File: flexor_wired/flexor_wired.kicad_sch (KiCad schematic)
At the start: 0 parts

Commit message: feat: add project metadata to KiCad files
- Add comments, revision, title and issue date to schematic and PCB
- Update project information for flexor_wired variant
- Update project information for flexor_wireless variant
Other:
- title: (none) -> Flexor Keyboard - Wired
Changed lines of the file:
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@@
 	(generator_version "9.0")
 	(paper "A4")
+	(title_block
+		(title "Flexor Keyboard - Wired")
+		(date "2025-08-14")
+		(rev "A")
+		(comment 1 "Wired Version")
+		(comment 2 "34-Key Split Ergonomic Keyboard")
+		(comment 4 "F L E X O R")
+	)
 	(sheet_instances
 		(path "/"

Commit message: feat: update PCB design and project configuration
- Update flexor_wired PCB layout and schematic
- Update project configuration and preferences
- Update footprint info cache
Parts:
- added D1, D10, D11, D12, D13, D14, D15, D16, D17, D18, D19, D2, D20, D21, D22, D23, D24, D25, D26, D27, D28, D29, D3, D30, D31, D32, D33, D34, D4, D5, D6, D7, D8, D9: 1N4148W, Diode:1N4148W_SOD-123_SMD, symbol Device:D_Small
- added H1, H2, H3, H4, H5, H6, H7, H8: MountingHole, Mounting_Hole:3.2mm_M3_DIN965_Pad, symbol Mechanical:MountingHole
- added SW1, SW10, SW11, SW12, SW13, SW14, SW15, SW16, SW17, SW18, SW19, SW2, SW20, SW21, SW22, SW23, SW24, SW25, SW26, SW27, SW28, SW29, SW3, SW30, SW31, SW32, SW33, SW34, SW4, SW5, SW6, SW7, SW8, SW9: PG1350, Kailh:PG1350_Choc_V1, symbol Switch:SW_Push
- added U1, U2: RP2040, Seed Studio:XIAO_RP2040_SMD, symbol Seed Studio:XIAO-RP2040-SMD
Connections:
- new net: D8.2 (A), SW8.2
- new net: D25.2 (A), SW25.2
- new net: D22.2 (A), SW22.2
- new net: D3.2 (A), SW3.2
- new net: D9.2 (A), SW9.2
- new net: D10.2 (A), SW10.2
- new net: D29.2 (A), SW29.2
- new net: D28.2 (A), SW28.2
- new net: D5.2 (A), SW5.2
- new net: D30.2 (A), SW30.2
- new net: D31.2 (A), SW31.2
- new net: D32.2 (A), SW32.2
- new net: D13.2 (A), SW13.2
- new net: D15.2 (A), SW15.2
- new net: D24.2 (A), SW24.2
- new net: D1.2 (A), SW1.2
- new net: D21.2 (A), SW21.2
- new net: D34.2 (A), SW34.2
- new net: D33.2 (A), SW33.2
- new net: D27.2 (A), SW27.2
- new net: D4.2 (A), SW4.2
- new net: D20.2 (A), SW20.2
- new net: D23.2 (A), SW23.2
- new net: D19.2 (A), SW19.2
- new net: D16.2 (A), SW16.2
- new net: D7.2 (A), SW7.2
- new net: D12.2 (A), SW12.2
- new net: D2.2 (A), SW2.2
- new net: D14.2 (A), SW14.2
- new net: D18.2 (A), SW18.2
- new net: D11.2 (A), SW11.2
- new net: D6.2 (A), SW6.2
- new net: D17.2 (A), SW17.2
- new net: D26.2 (A), SW26.2
- new net COL0_L: SW1.1, SW11.1, SW6.1, U1.5 (D4_SDA)
- new net COL0_R: SW22.1, SW27.1, SW32.1, U2.5 (D4_SDA)
- new net COL1_L: SW12.1, SW2.1, SW7.1, U1.6 (D5_SCL)
- new net COL1_R: SW21.1, SW26.1, SW31.1, U2.6 (D5_SCL)
- new net COL2_L: SW13.1, SW3.1, SW8.1, U1.11 (D10_MOSI)
- new net COL2_R: SW20.1, SW25.1, SW30.1, U2.11 (D10_MOSI)
- new net COL3_L: SW14.1, SW16.1, SW4.1, SW9.1, U1.10 (D9_MISO)
- new net COL3_R: SW19.1, SW24.1, SW29.1, SW34.1, U2.10 (D9_MISO)
- new net COL4_L: SW10.1, SW15.1, SW17.1, SW5.1, U1.9 (D8_SCK)
- new net COL4_R: SW18.1, SW23.1, SW28.1, SW33.1, U2.9 (D8_SCK)
- new net GND_L: U1.13 (GND)
- new net ROW0_L: D1.1 (K), D2.1 (K), D3.1 (K), D4.1 (K), D5.1 (K), U1.1 (D0)
- new net ROW0_R: D18.1 (K), D19.1 (K), D20.1 (K), D21.1 (K), D22.1 (K), U2.1 (D0)
- new net ROW1_L: D10.1 (K), D6.1 (K), D7.1 (K), D8.1 (K), D9.1 (K), U1.2 (D1)
- new net ROW1_R: D23.1 (K), D24.1 (K), D25.1 (K), D26.1 (K), D27.1 (K), U2.2 (D1)
- new net ROW2_L: D11.1 (K), D12.1 (K), D13.1 (K), D14.1 (K), D15.1 (K), U1.3 (D2)
- new net ROW2_R: D28.1 (K), D29.1 (K), D30.1 (K), D31.1 (K), D32.1 (K), U2.3 (D2)
- new net ROW3_L: D16.1 (K), D17.1 (K), U1.4 (D3)
- new net ROW3_R: D33.1 (K), D34.1 (K), U2.4 (D3)

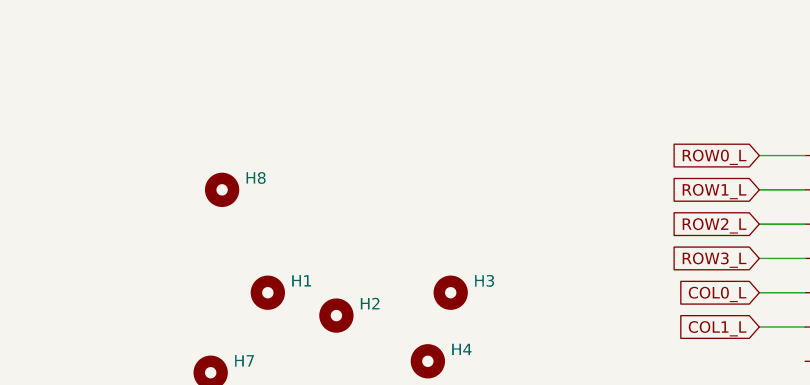
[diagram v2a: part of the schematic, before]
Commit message: feat(schematic): update schematic to support new keycap layout
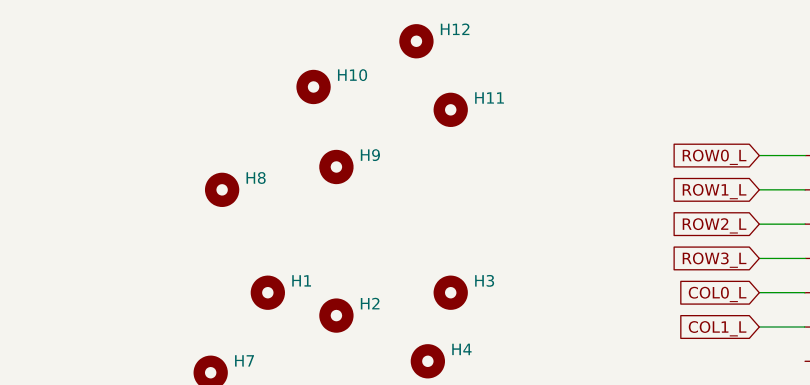
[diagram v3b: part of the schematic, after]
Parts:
- added H10, H11, H12, H9: MountingHole, Mounting_Hole:3.2mm_M3_DIN965_Pad, symbol Mechanical:MountingHole
